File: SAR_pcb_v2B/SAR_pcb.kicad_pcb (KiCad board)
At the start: 4 copper layers, 67.6 x 49.5 mm, 33 parts, among them J1 Conn_Coaxial_Power, J10 Conn_Coaxial, J2 Conn_Coaxial_Power, J3 Conn_02x10_Top_Bottom, J4 Conn_01x06, J9 Conn_Coaxial, SW1 SW_Push, U2 10B_SAR

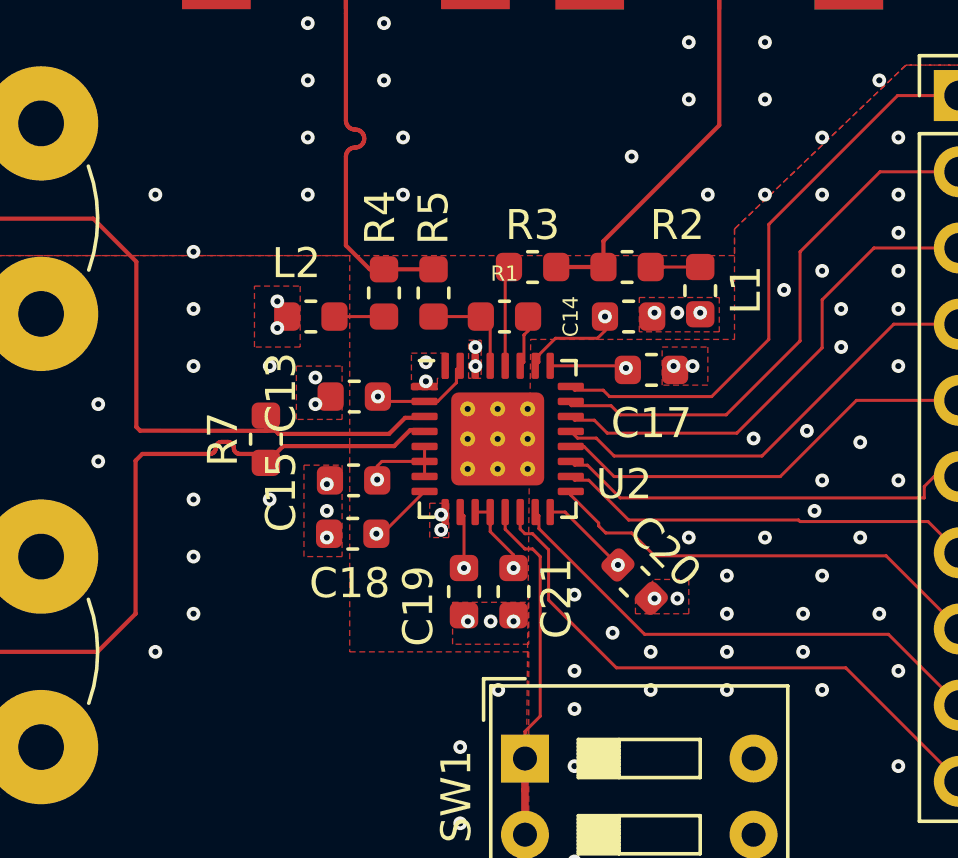
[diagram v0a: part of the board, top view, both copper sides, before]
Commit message: Made copy of v2 PCB without 50 Ohm terminations
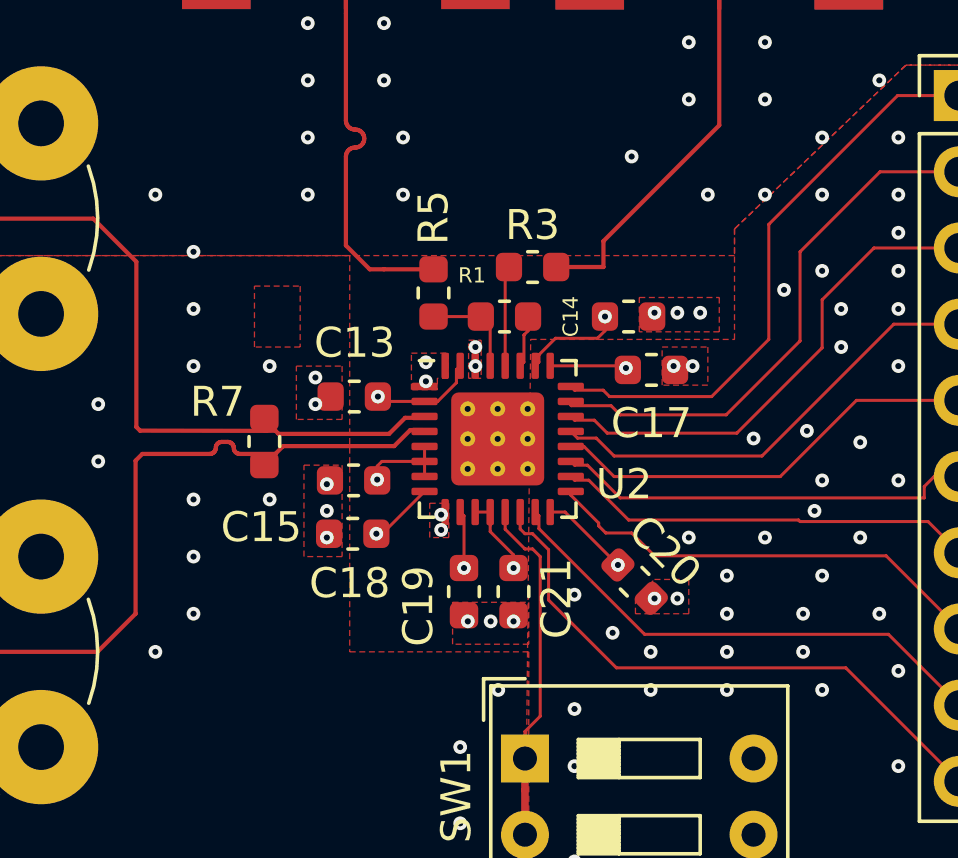
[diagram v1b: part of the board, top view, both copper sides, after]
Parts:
- removed L1: 1 nH, Inductor_SMD:L_0603_1608Metric
- removed L2: 2.2 nH, Inductor_SMD:L_0603_1608Metric
- removed R2, R4: 49.9, Resistor_SMD:R_0603_1608Metric
- moved R7 0.09 mm to (141.4, 93.3)
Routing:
- net Net-(L2-Pad1): track 1.65 -> 0.00 mm
- net Net-(L1-Pad1): track 1.65 -> 0.00 mm
- net VIN-: track 22.9 -> 22.4 mm
- net GND: vias 159 -> 156
